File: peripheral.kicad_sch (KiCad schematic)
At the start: 0 parts

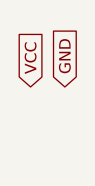
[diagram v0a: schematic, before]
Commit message: now using correct VCC and GND symbols
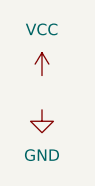
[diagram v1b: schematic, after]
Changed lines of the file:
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@@
 (kicad_sch (version 20211123) (generator eeschema)
   (paper "A4")
-  (global_label "GND" (shape input) (at 27.94 25.4 90) (fields_autoplaced)
-    (effects (font (size 1.27 1.27)) (justify left))
-    (property "Intersheet References" "${INTERSHEET_REFS}" (id 0) (at 27.8606 19.1164 90)
-      (effects (font (size 1.27 1.27)) (justify left) hide)
+  (symbol (lib_id "power:GND") (at 25.4 27.94 0) (unit 1)
+    (in_bom yes) (on_board yes) (fields_autoplaced)
+    (property "Reference" "#PWR?" (id 0) (at 25.4 34.29 0)
+      (effects (font (size 1.27 1.27)) hide)
     )
+    (property "Value" "GND" (id 1) (at 25.4 33.02 0))
+    (property "Footprint" "" (id 2) (at 25.4 27.94 0)
+      (effects (font (size 1.27 1.27)) hide)
+    )
+    (property "Datasheet" "" (id 3) (at 25.4 27.94 0)
+      (effects (font (size 1.27 1.27)) hide)
+    )
+    (pin "1")
   )
-  (global_label "VCC" (shape input) (at 24.13 25.4 90) (fields_autoplaced)
-    (effects (font (size 1.27 1.27)) (justify left))
-    (property "Intersheet References" "${INTERSHEET_REFS}" (id 0) (at 24.0506 19.3583 90)
-      (effects (font (size 1.27 1.27)) (justify left) hide)
+  (symbol (lib_id "power:VCC") (at 25.4 24.13 0) (unit 1)
+    (in_bom yes) (on_board yes) (fields_autoplaced)
+    (property "Reference" "#PWR?" (id 0) (at 25.4 27.94 0)
+      (effects (font (size 1.27 1.27)) hide)
     )
+    (property "Value" "VCC" (id 1) (at 25.4 19.05 0))
+    (property "Footprint" "" (id 2) (at 25.4 24.13 0)
+      (effects (font (size 1.27 1.27)) hide)
+    )
+    (property "Datasheet" "" (id 3) (at 25.4 24.13 0)
+      (effects (font (size 1.27 1.27)) hide)
+    )
+    (pin "1")
   )
 )

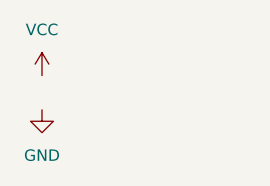
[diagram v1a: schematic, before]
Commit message: added esp32 schematic && updated supply symbols
Signed-off-by: Tobias Gent <gent.tobias@gmail.com>
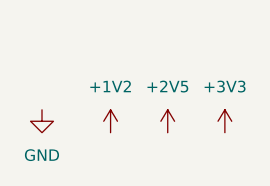
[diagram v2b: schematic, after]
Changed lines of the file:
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@@
 (kicad_sch (version 20211123) (generator eeschema)
   (paper "A4")
+  (symbol (lib_id "power:+2V5") (at 39.37 30.48 0) (unit 1)
+    (in_bom yes) (on_board yes) (fields_autoplaced)
+    (property "Reference" "#PWR?" (id 0) (at 39.37 34.29 0)
+      (effects (font (size 1.27 1.27)) hide)
+    )
+    (property "Value" "+2V5" (id 1) (at 39.37 25.4 0))
+    (property "Footprint" "" (id 2) (at 39.37 30.48 0)
+      (effects (font (size 1.27 1.27)) hide)
+    )
+    (property "Datasheet" "" (id 3) (at 39.37 30.48 0)
+      (effects (font (size 1.27 1.27)) hide)
+    )
+    (pin "1")
+  )
+  (symbol (lib_id "power:+3V3") (at 45.72 30.48 0) (unit 1)
+    (in_bom yes) (on_board yes) (fields_autoplaced)
+    (property "Reference" "#PWR?" (id 0) (at 45.72 34.29 0)
+      (effects (font (size 1.27 1.27)) hide)
+    )
+    (property "Value" "+3V3" (id 1) (at 45.72 25.4 0))
+    (property "Footprint" "" (id 2) (at 45.72 30.48 0)
+      (effects (font (size 1.27 1.27)) hide)
+    )
+    (property "Datasheet" "" (id 3) (at 45.72 30.48 0)
+      (effects (font (size 1.27 1.27)) hide)
+    )
+    (pin "1")
+  )
+  (symbol (lib_id "power:+1V2") (at 33.02 30.48 0) (unit 1)
+    (in_bom yes) (on_board yes) (fields_autoplaced)
+    (property "Reference" "#PWR?" (id 0) (at 33.02 34.29 0)
+      (effects (font (size 1.27 1.27)) hide)
+    )
+    (property "Value" "+1V2" (id 1) (at 33.02 25.4 0))
+    (property "Footprint" "" (id 2) (at 33.02 30.48 0)
+      (effects (font (size 1.27 1.27)) hide)
+    )
+    (property "Datasheet" "" (id 3) (at 33.02 30.48 0)
+      (effects (font (size 1.27 1.27)) hide)
+    )
+    (pin "1")
+  )
   (symbol (lib_id "power:GND") (at 25.4 27.94 0) (unit 1)
     (in_bom yes) (on_board yes) (fields_autoplaced)
@@
       (effects (font (size 1.27 1.27)) hide)
     )
-    (pin "1")
-  )
-  (symbol (lib_id "power:VCC") (at 25.4 24.13 0) (unit 1)
-    (in_bom yes) (on_board yes) (fields_autoplaced)
-    (property "Reference" "#PWR?" (id 0) (at 25.4 27.94 0)
-      (effects (font (size 1.27 1.27)) hide)
-    )
-    (property "Value" "VCC" (id 1) (at 25.4 19.05 0))
-    (property "Footprint" "" (id 2) (at 25.4 24.13 0)
-      (effects (font (size 1.27 1.27)) hide)
-    )
-    (property "Datasheet" "" (id 3) (at 25.4 24.13 0)
-      (effects (font (size 1.27 1.27)) hide)
-    )
